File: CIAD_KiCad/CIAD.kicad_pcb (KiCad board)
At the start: 2 copper layers, 23 parts, among them J2 Conn_01x08, SW1 SW_Push, SW10 SW_Push, SW11 SW_Push, SW2 SW_Push, SW3 SW_Push, SW4 SW_Push, SW5 SW_Push, SW6 SW_Push, SW7 SW_Push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

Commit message: Added new libraries for hardware, updated the hardware part
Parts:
- added D10: LED_Dual_AKA, LED_THT:LED_D5.0mm-3, F.Cu at (57.0, 160.5)
- added D11: ~, CIAD:44pin_screen, F.Cu at (136.0, 51.6)
- moved D1 90.1 mm to (77.6, 150.1)
- moved SW1 90.1 mm to (131.0, 130.3)
- moved SW2 90.1 mm to (115.5, 144.0)
- moved SW3 90.1 mm to (144.3, 143.7)
- moved SW4 90.1 mm to (131.0, 156.0)
- moved SW5 90.1 mm to (131.0, 143.5)
- moved SW6 90.1 mm to (149.3, 158.2)
- moved A1 90.1 mm to (100.0, 92.1)
- moved D2 90.1 mm to (77.4, 160.6)
- moved D3 90.1 mm to (77.4, 170.6)
- moved D4 90.1 mm to (87.4, 150.1)
- moved D5 90.1 mm to (87.4, 160.5)
- moved D6 90.1 mm to (87.4, 170.6)
- moved D7 90.1 mm to (96.9, 150.1)
- moved D8 90.1 mm to (96.9, 160.5)
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
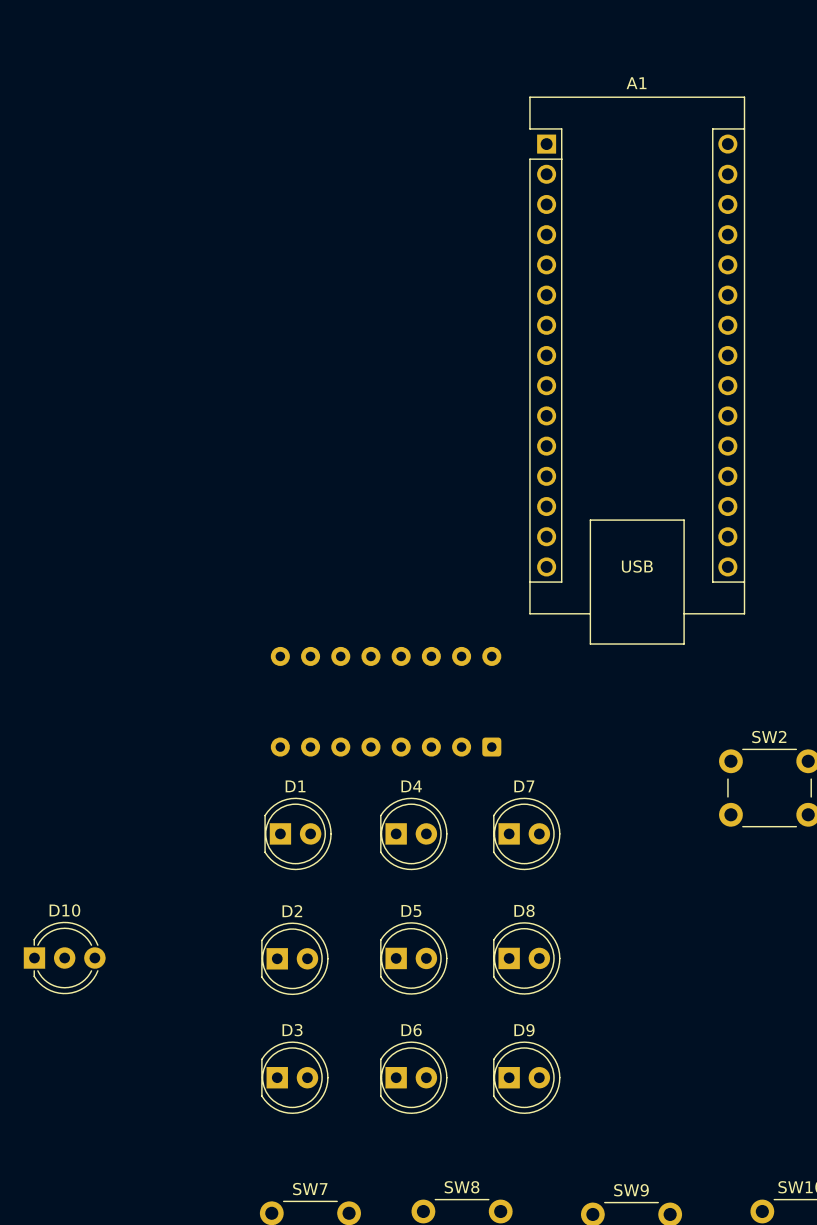
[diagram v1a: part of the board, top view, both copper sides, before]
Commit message: updated .gitignore, replaced LEDs in /hardware and fixed connections
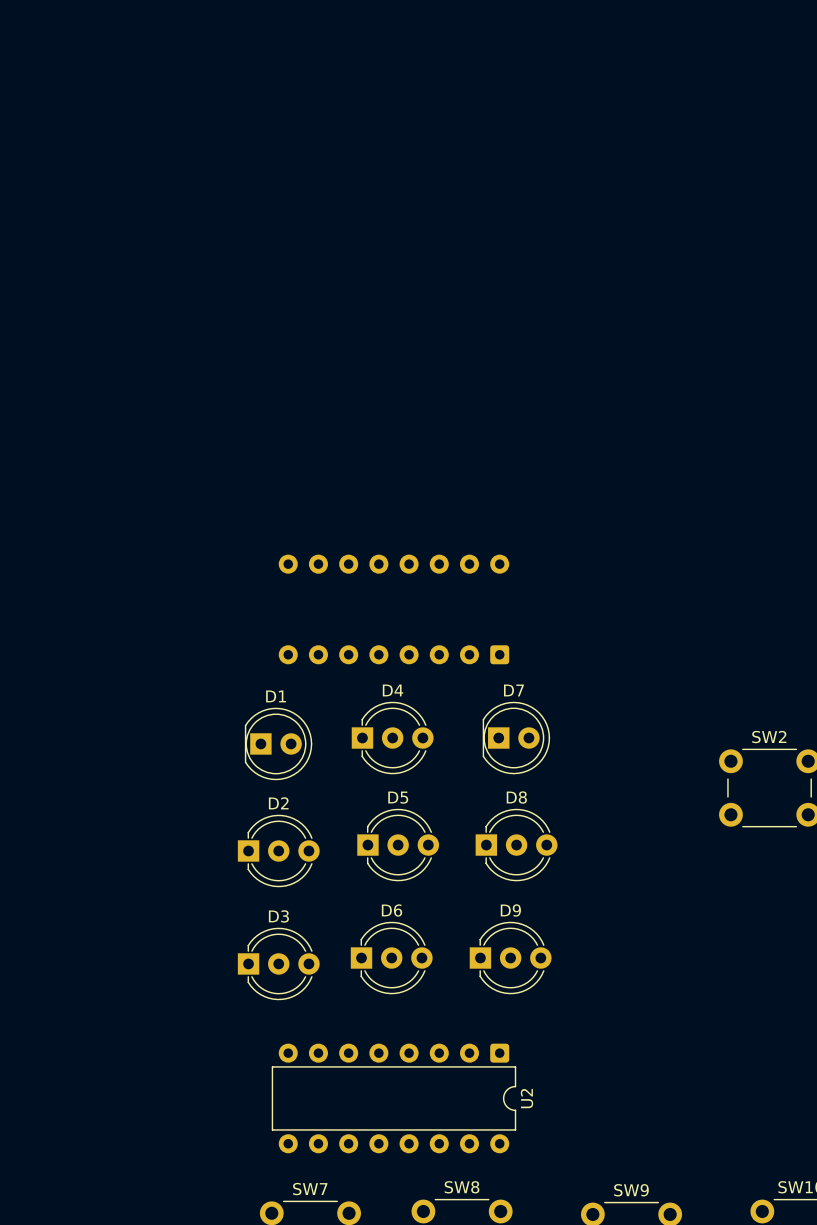
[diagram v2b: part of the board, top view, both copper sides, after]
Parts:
- removed A1: Arduino_Nano_v3.x, Module:Arduino_Nano
- removed D10: LED_Dual_AKA, LED_THT:LED_D5.0mm-3
- added U2: 74HC595, Package_DIP:DIP-16_W7.62mm, F.Cu at (96.1, 168.5)
- D2, D3, D4, D5, D6, D8, D9: value LED -> LED_Dual_AKA; footprint LED_THT:LED_D5.0mm -> LED_THT:LED_D5.0mm-3
- moved D6 10.5 mm to (84.5, 160.5)
- moved D9 10.4 mm to (94.5, 160.5)
- moved D3 9.87 mm to (75.0, 161.0)
- moved D5 9.83 mm to (85.0, 151.0)
- moved D8 9.73 mm to (95.0, 151.0)
- moved D2 9.38 mm to (75.0, 151.5)
- moved D4 8.55 mm to (84.5, 142.0)
- moved D7 8.11 mm to (96.0, 142.0)
- moved U1 7.79 mm to (96.1, 135.0)
- moved D1 7.74 mm to (76.0, 142.5)
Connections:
- D11 pad 12: unconnected-(D11-RESET-Pad12) -> /SCR_RST
- D11 pad 15: unconnected-(D11-DB15-Pad15) -> /DB15
- D11 pad 16: unconnected-(D11-DB16-Pad16) -> /DB16
- D11 pad 17: unconnected-(D11-DB17-Pad17) -> /DB17
- D11 pad 18: unconnected-(D11-DB18-Pad18) -> /DB18
- D11 pad 19: unconnected-(D11-DB19-Pad19) -> /DB19
- D11 pad 20: unconnected-(D11-DB20-Pad20) -> /DB20
- D11 pad 21: unconnected-(D11-DB21-Pad21) -> /DB21
- D11 pad 22: unconnected-(D11-DB22-Pad22) -> /DB22
- D11 pad 23: unconnected-(D11-DB23-Pad23) -> /DB23
- D11 pad 24: unconnected-(D11-DB24-Pad24) -> /DB24
- D11 pad 25: unconnected-(D11-DB25-Pad25) -> /DB25
- D11 pad 26: unconnected-(D11-DB26-Pad26) -> /DB26
- D11 pad 27: unconnected-(D11-DB27-Pad27) -> /DB27
- D11 pad 28: unconnected-(D11-DB28-Pad28) -> /DB28
- D11 pad 29: unconnected-(D11-DB29-Pad29) -> /DB29
- D11 pad 30: unconnected-(D11-DB30-Pad30) -> /DB30
- D2 pad 1: GND -> /LED2_G
- D2 pad 2: /LED2 -> GND
- D3 pad 1: GND -> /LED3_G
- D3 pad 2: /LED3 -> GND
- D4 pad 1: GND -> /LED4_G
- D4 pad 2: /LED4 -> GND
- D5 pad 1: GND -> /LED5_G
- D5 pad 2: /LED5 -> GND
- D6 pad 1: GND -> /LED6_G
- D6 pad 2: /LED6 -> GND
- D8 pad 1: GND -> /LED8_G
- D8 pad 2: /LED8 -> GND
- D9 pad 1: GND -> /LED9_G
- D9 pad 2: Net-(A1-D2) -> GND
- U1 pad 1: /LED2 -> /LED5_B
- U1 pad 10: Net-(A1-A1) -> unconnected-(U1-~{SRCLR}-Pad10)
- U1 pad 11: /CLK -> unconnected-(U1-SRCLK-Pad11)
- U1 pad 13: Net-(A1-A0) -> unconnected-(U1-~{OE}-Pad13)
- U1 pad 14: /MOSI -> unconnected-(U1-SER-Pad14)
- U1 pad 15: /LED1 -> /LED7
- U1 pad 2: /LED3 -> /LED5_G
- U1 pad 3: /LED4 -> /LED4_B
- U1 pad 4: /LED5 -> /LED4_G
- U1 pad 5: /LED6 -> /LED2_B
- U1 pad 6: /LED7 -> /LED2_G
- U1 pad 7: /LED8 -> /LED1

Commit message: small updates to hardware
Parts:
- added REF**: ESP32, CIAD:ESP32, F.Cu at (113.0, 98.0)
